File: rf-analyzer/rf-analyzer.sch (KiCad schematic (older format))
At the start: 59 parts, among them U1 AD8302, U2 AD8302, U3 OPA695

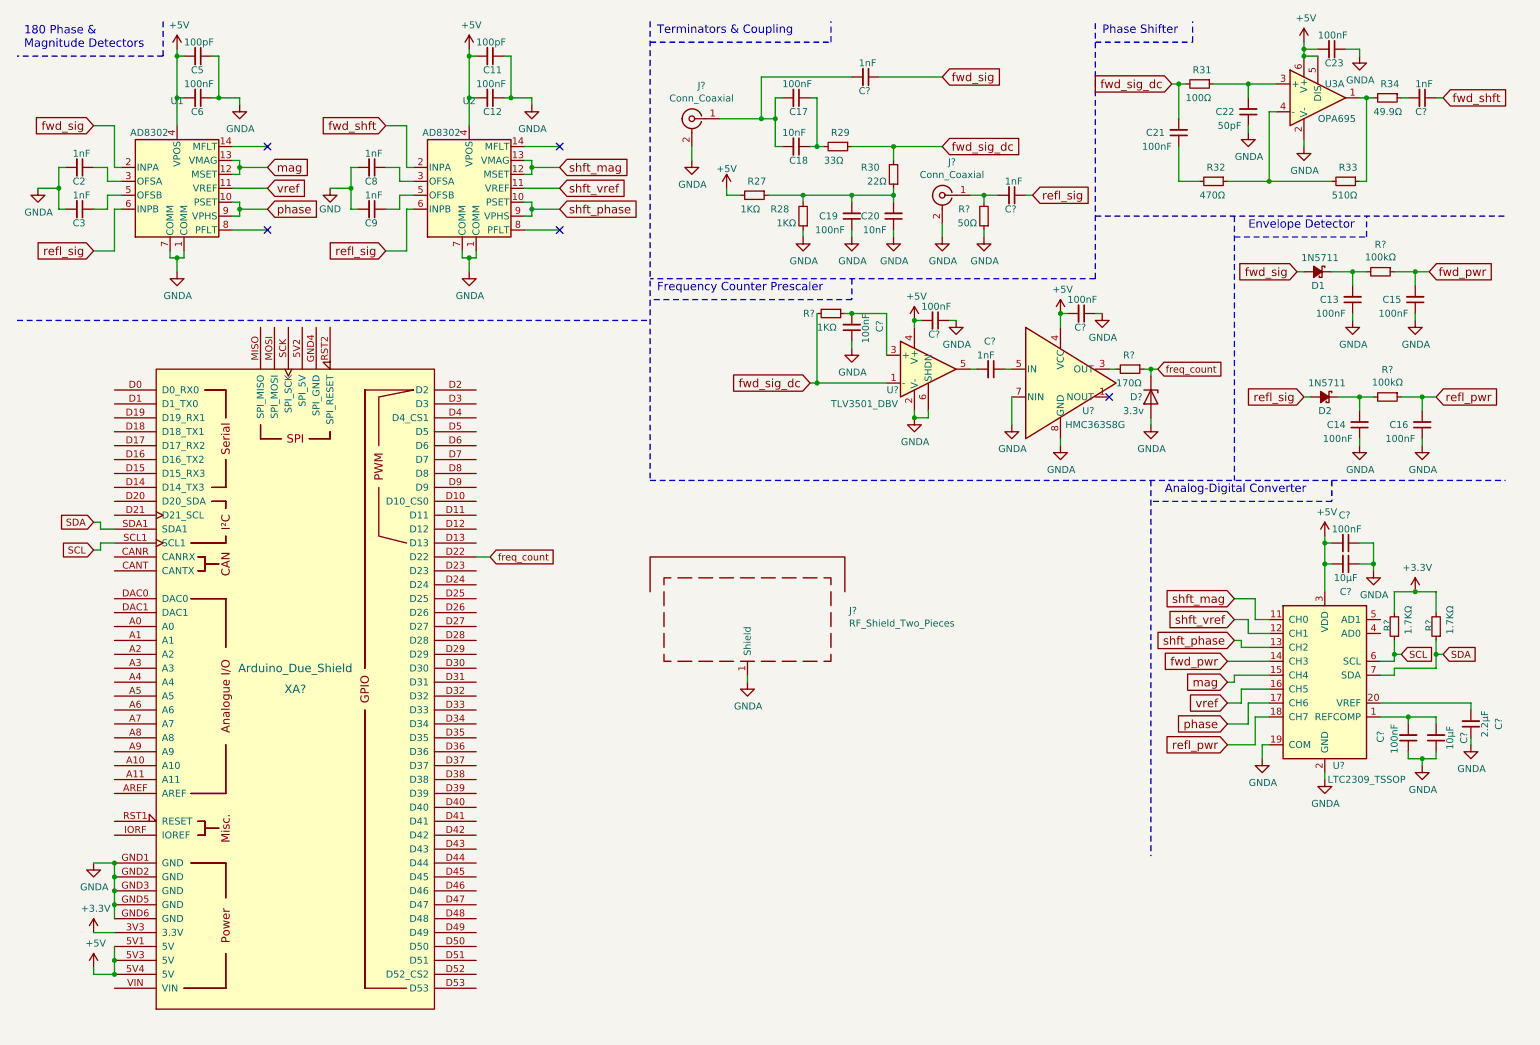
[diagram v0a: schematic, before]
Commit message: Removed the enumeration of the components, will re-add later5.
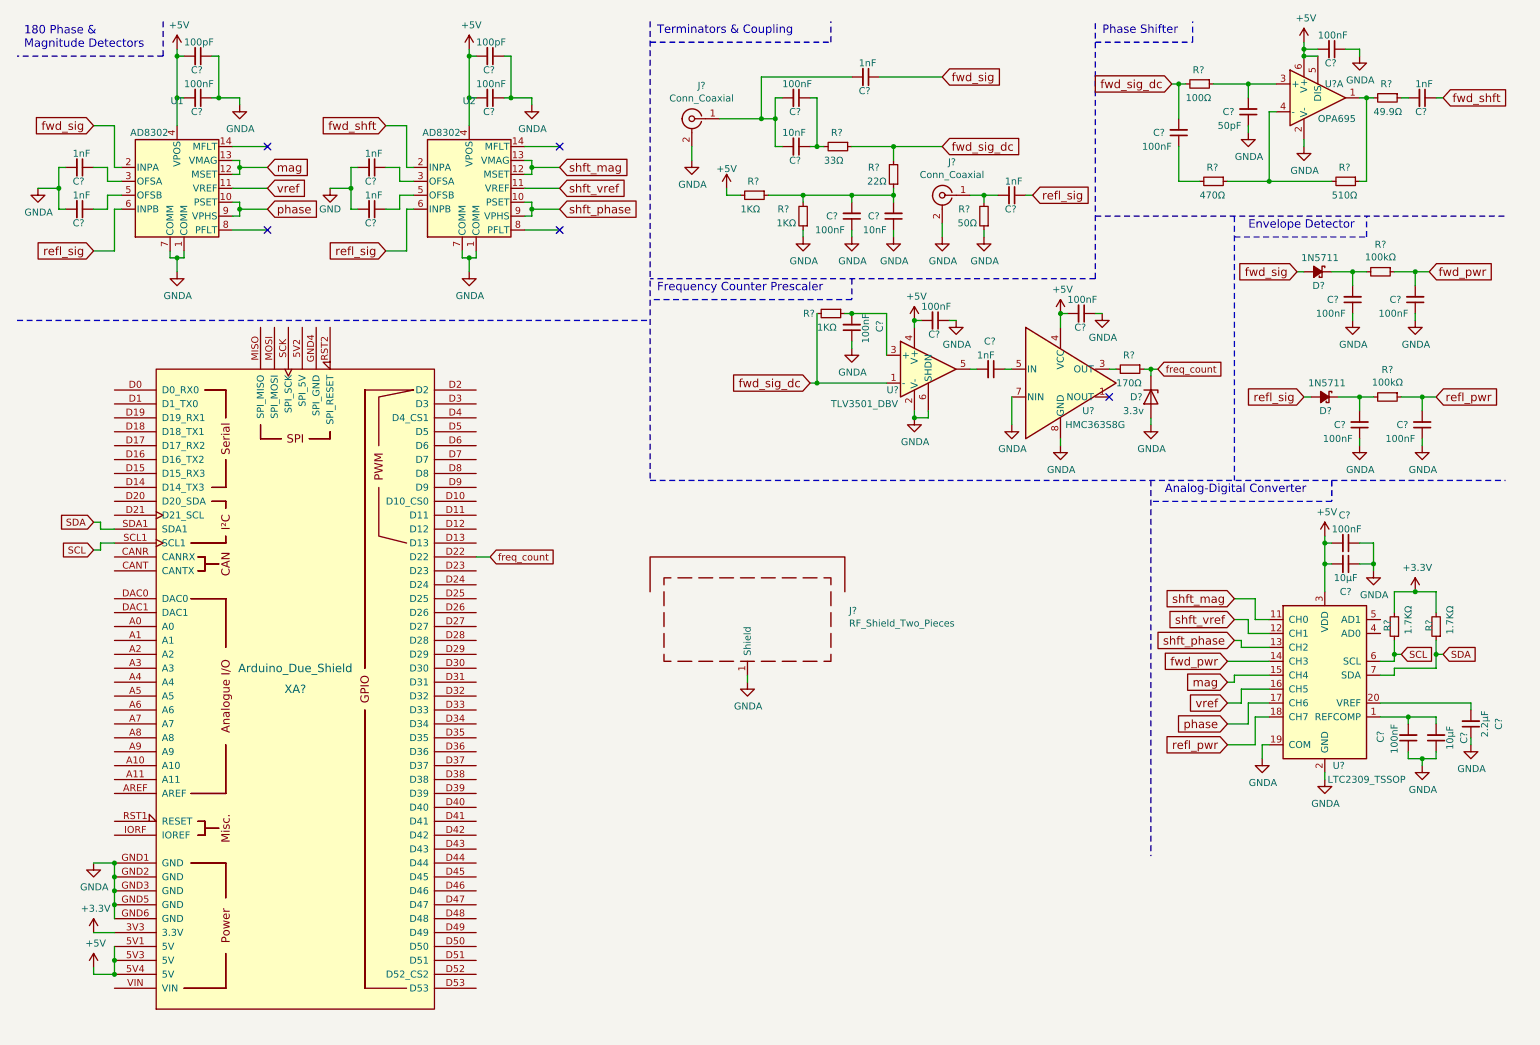
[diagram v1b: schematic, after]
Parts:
- renumbered C23 to C?, C21 to C?, C22 to C?, C18 to C?, C17 to C?, C20 to C?, C19 to C?, C13 to C?, C15 to C?, C14 to C?, C16 to C?, C2 to C?, C3 to C?, C6 to C?, C5 to C?, C8 to C?, C9 to C?, C12 to C?, C11 to C?, D1 to D?, D2 to D?, R33 to R?, R34 to R?, R32 to R?, R31 to R?, R30 to R?, R29 to R?, R28 to R?, R27 to R?, U3 to U?
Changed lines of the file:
@@
 $EndDescr
 $Comp
-L Device:R_Small R33
+L Device:R_Small R?
 U 1 1 596FDF71
 P 10050 1650
-F 0 "R33" V 9950 1600 50  0000 L CNN
+F 0 "R?" V 9950 1600 50  0000 L CNN
 F 1 "510Ω" V 10150 1550 50  0000 L CNN
 F 2 "Resistor_SMD:R_0603_1608Metric_Pad1.05x0.95mm_HandSolder" H 10050 1650 50  0001 C CNN
@@
 $EndComp
 $Comp
-L Device:R_Small R34
+L Device:R_Small R?
 U 1 1 596FEB83
 P 10350 1050
-F 0 "R34" V 10250 1000 50  0000 L CNN
+F 0 "R?" V 10250 1000 50  0000 L CNN
 F 1 "49.9Ω" V 10450 950 50  0000 L CNN
 F 2 "Resistor_SMD:R_0603_1608Metric_Pad1.05x0.95mm_HandSolder" H 10350 1050 50  0001 C CNN
@@
 $EndComp
 $Comp
-L Device:C_Small C23
+L Device:C_Small C?
 U 1 1 596FF084
 P 9950 700
-F 0 "C23" V 10050 650 50  0000 L CNN
+F 0 "C?" V 10050 650 50  0000 L CNN
 F 1 "100nF" V 9850 600 50  0000 L CNN
 F 2 "Capacitor_SMD:C_0603_1608Metric_Pad1.05x0.95mm_HandSolder" H 9950 700 50  0001 C CNN
@@
 $EndComp
 $Comp
-L Device:R_Small R32
+L Device:R_Small R?
 U 1 1 59705BB2
 P 9100 1650
-F 0 "R32" V 9000 1600 50  0000 L CNN
+F 0 "R?" V 9000 1600 50  0000 L CNN
 F 1 "470Ω" V 9200 1550 50  0000 L CNN
 F 2 "Resistor_SMD:R_0603_1608Metric_Pad1.05x0.95mm_HandSolder" H 9100 1650 50  0001 C CNN
@@
 $EndComp
 $Comp
-L Device:C_Small C21
+L Device:C_Small C?
 U 1 1 59705C59
 P 8850 1300
-F 0 "C21" H 8950 1300 50  0000 L CNN
+F 0 "C?" H 8950 1300 50  0000 L CNN
 F 1 "100nF" H 8900 1400 50  0000 L CNN
 F 2 "Capacitor_SMD:C_0603_1608Metric_Pad1.05x0.95mm_HandSolder" H 8850 1300 50  0001 C CNN
@@
 $EndComp
 $Comp
-L Device:C_Small C22
+L Device:C_Small C?
 U 1 1 59706A4C
 P 9350 1150
-F 0 "C22" H 9450 1150 50  0000 L CNN
+F 0 "C?" H 9450 1150 50  0000 L CNN
 F 1 "50pF" H 9400 1250 50  0000 L CNN
 F 2 "Capacitor_SMD:C_0603_1608Metric_Pad1.05x0.95mm_HandSolder" H 9350 1150 50  0001 C CNN
@@
 $EndComp
 $Comp
-L Device:R_Small R31
+L Device:R_Small R?
 U 1 1 59706B15
 P 9000 950
-F 0 "R31" V 8900 900 50  0000 L CNN
+F 0 "R?" V 8900 900 50  0000 L CNN
 F 1 "100Ω" V 9100 850 50  0000 L CNN
 F 2 "Resistor_SMD:R_0603_1608Metric_Pad1.05x0.95mm_HandSolder" H 9000 950 50  0001 C CNN
@@
 $EndComp
 $Comp
-L Device:R_Small R30
+L Device:R_Small R?
 U 1 1 59707359
 P 6800 1600
-F 0 "R30" H 6900 1550 50  0000 L CNN
+F 0 "R?" H 6900 1550 50  0000 L CNN
 F 1 "22Ω" H 6850 1650 50  0000 L CNN
 F 2 "Resistor_SMD:R_0603_1608Metric_Pad1.05x0.95mm_HandSolder" H 6800 1600 50  0001 C CNN
@@
 $EndComp
 $Comp
-L Device:R_Small R29
+L Device:R_Small R?
 U 1 1 597076A4
 P 6400 1400
-F 0 "R29" V 6300 1350 50  0000 L CNN
+F 0 "R?" V 6300 1350 50  0000 L CNN
 F 1 "33Ω" V 6500 1300 50  0000 L CNN
 F 2 "Resistor_SMD:R_0603_1608Metric_Pad1.05x0.95mm_HandSolder" H 6400 1400 50  0001 C CNN
@@
 $EndComp
 $Comp
-L Device:C_Small C18
+L Device:C_Small C?
 U 1 1 59707E9F
 P 6100 1400
-F 0 "C18" V 6200 1350 50  0000 L CNN
+F 0 "C?" V 6200 1350 50  0000 L CNN
 F 1 "10nF" V 6000 1300 50  0000 L CNN
 F 2 "Capacitor_SMD:C_0603_1608Metric_Pad1.05x0.95mm_HandSolder" H 6100 1400 50  0001 C CNN
@@
 $EndComp
 $Comp
-L Device:C_Small C20
+L Device:C_Small C?
 U 1 1 59708773
 P 6800 1900
-F 0 "C20" H 6900 1900 50  0000 L CNN
+F 0 "C?" H 6900 1900 50  0000 L CNN
 F 1 "10nF" H 6850 2000 50  0000 L CNN
 F 2 "Capacitor_SMD:C_0603_1608Metric_Pad1.05x0.95mm_HandSolder" H 6800 1900 50  0001 C CNN
@@
 $EndComp
 $Comp
-L Device:C_Small C19
+L Device:C_Small C?
 U 1 1 597087DD
 P 6500 1900
-F 0 "C19" H 6600 1900 50  0000 L CNN
+F 0 "C?" H 6600 1900 50  0000 L CNN
 F 1 "100nF" H 6550 2000 50  0000 L CNN
 F 2 "Capacitor_SMD:C_0603_1608Metric_Pad1.05x0.95mm_HandSolder" H 6500 1900 50  0001 C CNN
@@
 $EndComp
 $Comp
-L Device:R_Small R28
+L Device:R_Small R?
 U 1 1 597088B3
 P 6150 1900
-F 0 "R28" H 6250 1850 50  0000 L CNN
+F 0 "R?" H 6250 1850 50  0000 L CNN
 F 1 "1KΩ" H 6200 1950 50  0000 L CNN
 F 2 "Resistor_SMD:R_0603_1608Metric_Pad1.05x0.95mm_HandSolder" H 6150 1900 50  0001 C CNN
@@
 $EndComp
 $Comp
-L Device:R_Small R27
+L Device:R_Small R?
 U 1 1 59708D55
 P 5800 1750
-F 0 "R27" V 5700 1700 50  0000 L CNN
+F 0 "R?" V 5700 1700 50  0000 L CNN
 F 1 "1KΩ" V 5900 1650 50  0000 L CNN
 F 2 "Resistor_SMD:R_0603_1608Metric_Pad1.05x0.95mm_HandSolder" H 5800 1750 50  0001 C CNN
@@
 Phase Shifter
 $Comp
-L Device:D_Schottky_Small_ALT D1
+L Device:D_Schottky_Small_ALT D?
 U 1 1 5970BBB4
 P 9850 2300
-F 0 "D1" H 9800 2200 50  0000 L CNN
+F 0 "D?" H 9800 2200 50  0000 L CNN
 F 1 "1N5711" H 9700 2400 50  0000 L CNN
 F 2 "Diode_SMD:D_SMA" V 9850 2300 50  0001 C CNN
@@
 $EndComp
 $Comp
-L Device:C_Small C13
+L Device:C_Small C?
 U 1 1 5970BF1F
 P 10100 2500
-F 0 "C13" H 10200 2500 50  0000 L CNN
+F 0 "C?" H 10200 2500 50  0000 L CNN
 F 1 "100nF" H 10150 2600 50  0000 L CNN
 F 2 "Capacitor_SMD:C_0603_1608Metric_Pad1.05x0.95mm_HandSolder" H 10100 2500 50  0001 C CNN
@@
 $EndComp
 $Comp
-L Device:C_Small C15
+L Device:C_Small C?
 U 1 1 5970C0BE
 P 10550 2500
-F 0 "C15" H 10650 2500 50  0000 L CNN
+F 0 "C?" H 10650 2500 50  0000 L CNN
 F 1 "100nF" H 10600 2600 50  0000 L CNN
 F 2 "Capacitor_SMD:C_0603_1608Metric_Pad1.05x0.95mm_HandSolder" H 10550 2500 50  0001 C CNN
@@
 fwd_pwr
 $Comp
-L Device:D_Schottky_Small_ALT D2
+L Device:D_Schottky_Small_ALT D?
 U 1 1 5970EE87
 P 9900 3200
-F 0 "D2" H 9850 3100 50  0000 L CNN
+F 0 "D?" H 9850 3100 50  0000 L CNN
 F 1 "1N5711" H 9750 3300 50  0000 L CNN
 F 2 "Diode_SMD:D_SMA" V 9900 3200 50  0001 C CNN
@@
 $EndComp
 $Comp
-L Device:C_Small C14
+L Device:C_Small C?
 U 1 1 5970EE8D
 P 10150 3400
-F 0 "C14" H 10250 3400 50  0000 L CNN
+F 0 "C?" H 10250 3400 50  0000 L CNN
 F 1 "100nF" H 10200 3500 50  0000 L CNN
 F 2 "Capacitor_SMD:C_0603_1608Metric_Pad1.05x0.95mm_HandSolder" H 10150 3400 50  0001 C CNN
@@
 $EndComp
 $Comp
-L Device:C_Small C16
+L Device:C_Small C?
 U 1 1 5970EE93
 P 10600 3400
-F 0 "C16" H 10700 3400 50  0000 L CNN
+F 0 "C?" H 10700 3400 50  0000 L CNN
 F 1 "100nF" H 10650 3500 50  0000 L CNN
 F 2 "Capacitor_SMD:C_0603_1608Metric_Pad1.05x0.95mm_HandSolder" H 10600 3400 50  0001 C CNN
@@
 Envelope Detector
 $Comp
-L Device:C_Small C2
+L Device:C_Small C?
 U 1 1 5971253A
 P 950 1550
-F 0 "C2" V 1050 1500 50  0000 L CNN
+F 0 "C?" V 1050 1500 50  0000 L CNN
 F 1 "1nF" V 850 1500 50  0000 L CNN
 F 2 "Capacitor_SMD:C_0603_1608Metric_Pad1.05x0.95mm_HandSolder" H 950 1550 50  0001 C CNN
@@
 $EndComp
 $Comp
-L Device:C_Small C3
+L Device:C_Small C?
 U 1 1 597125A5
 P 950 1850
-F 0 "C3" V 1050 1800 50  0000 L CNN
+F 0 "C?" V 1050 1800 50  0000 L CNN
 F 1 "1nF" V 850 1800 50  0000 L CNN
 F 2 "Capacitor_SMD:C_0603_1608Metric_Pad1.05x0.95mm_HandSolder" H 950 1850 50  0001 C CNN
@@
 $EndComp
 $Comp
-L Device:C_Small C6
+L Device:C_Small C?
 U 1 1 59713489
 P 1800 1050
-F 0 "C6" V 1900 1000 50  0000 L CNN
+F 0 "C?" V 1900 1000 50  0000 L CNN
 F 1 "100nF" V 1700 950 50  0000 L CNN
 F 2 "Capacitor_SMD:C_0603_1608Metric_Pad1.05x0.95mm_HandSolder" H 1800 1050 50  0001 C CNN
@@
 $EndComp
 $Comp
-L Device:C_Small C5
+L Device:C_Small C?
 U 1 1 59713736
 P 1800 750
-F 0 "C5" V 1900 700 50  0000 L CNN
+F 0 "C?" V 1900 700 50  0000 L CNN
 F 1 "100pF" V 1700 650 50  0000 L CNN
 F 2 "Capacitor_SMD:C_0603_1608Metric_Pad1.05x0.95mm_HandSolder" H 1800 750 50  0001 C CNN
@@
 refl_sig
 $Comp
-L Device:C_Small C8
+L Device:C_Small C?
 U 1 1 59715DA1
 P 3050 1550
-F 0 "C8" V 3150 1500 50  0000 L CNN
+F 0 "C?" V 3150 1500 50  0000 L CNN
 F 1 "1nF" V 2950 1500 50  0000 L CNN
 F 2 "Capacitor_SMD:C_0603_1608Metric_Pad1.05x0.95mm_HandSolder" H 3050 1550 50  0001 C CNN
@@
 $EndComp
 $Comp
-L Device:C_Small C9
+L Device:C_Small C?
 U 1 1 59715DA7
 P 3050 1850
-F 0 "C9" V 3150 1800 50  0000 L CNN
+F 0 "C?" V 3150 1800 50  0000 L CNN
 F 1 "1nF" V 2950 1800 50  0000 L CNN
 F 2 "Capacitor_SMD:C_0603_1608Metric_Pad1.05x0.95mm_HandSolder" H 3050 1850 50  0001 C CNN
@@
 $EndComp
 $Comp
-L Device:C_Small C12
+L Device:C_Small C?
 U 1 1 59715DE8
 P 3900 1050
-F 0 "C12" V 4000 1000 50  0000 L CNN
+F 0 "C?" V 4000 1000 50  0000 L CNN
 F 1 "100nF" V 3800 950 50  0000 L CNN
 F 2 "Capacitor_SMD:C_0603_1608Metric_Pad1.05x0.95mm_HandSolder" H 3900 1050 50  0001 C CNN
@@
 $EndComp
 $Comp
-L Device:C_Small C11
+L Device:C_Small C?
 U 1 1 59715DF4
 P 3900 750
-F 0 "C11" V 4000 700 50  0000 L CNN
+F 0 "C?" V 4000 700 50  0000 L CNN
 F 1 "100pF" V 3800 650 50  0000 L CNN
 F 2 "Capacitor_SMD:C_0603_1608Metric_Pad1.05x0.95mm_HandSolder" H 3900 750 50  0001 C CNN
@@
 $EndComp
 $Comp
-L Amplifier_Operational_Freemo:OPA695 U3
+L Amplifier_Operational_Freemo:OPA695 U?
 U 1 1 5C3F18FF
 P 9850 1050
-F 0 "U3" H 9900 1150 50  0000 L CNN
+F 0 "U?" H 9900 1150 50  0000 L CNN
 F 1 "OPA695" H 9850 900 50  0000 L CNN
 F 2 "Package_TO_SOT_SMD:SOT-23-6" H 9750 1100 50  0001 C CNN
@@
 	6200 1050 6250 1050
 $Comp
-L Device:C_Small C17
+L Device:C_Small C?
 U 1 1 59707F0B
 P 6100 1050
-F 0 "C17" V 6200 1000 50  0000 L CNN
+F 0 "C?" V 6200 1000 50  0000 L CNN
 F 1 "100nF" V 6000 950 50  0000 L CNN
 F 2 "Capacitor_SMD:C_0603_1608Metric_Pad1.05x0.95mm_HandSolder" H 6100 1050 50  0001 C CNN
